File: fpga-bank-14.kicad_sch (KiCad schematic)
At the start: 1 part, among them U1 XC7K410T-2FFG900I

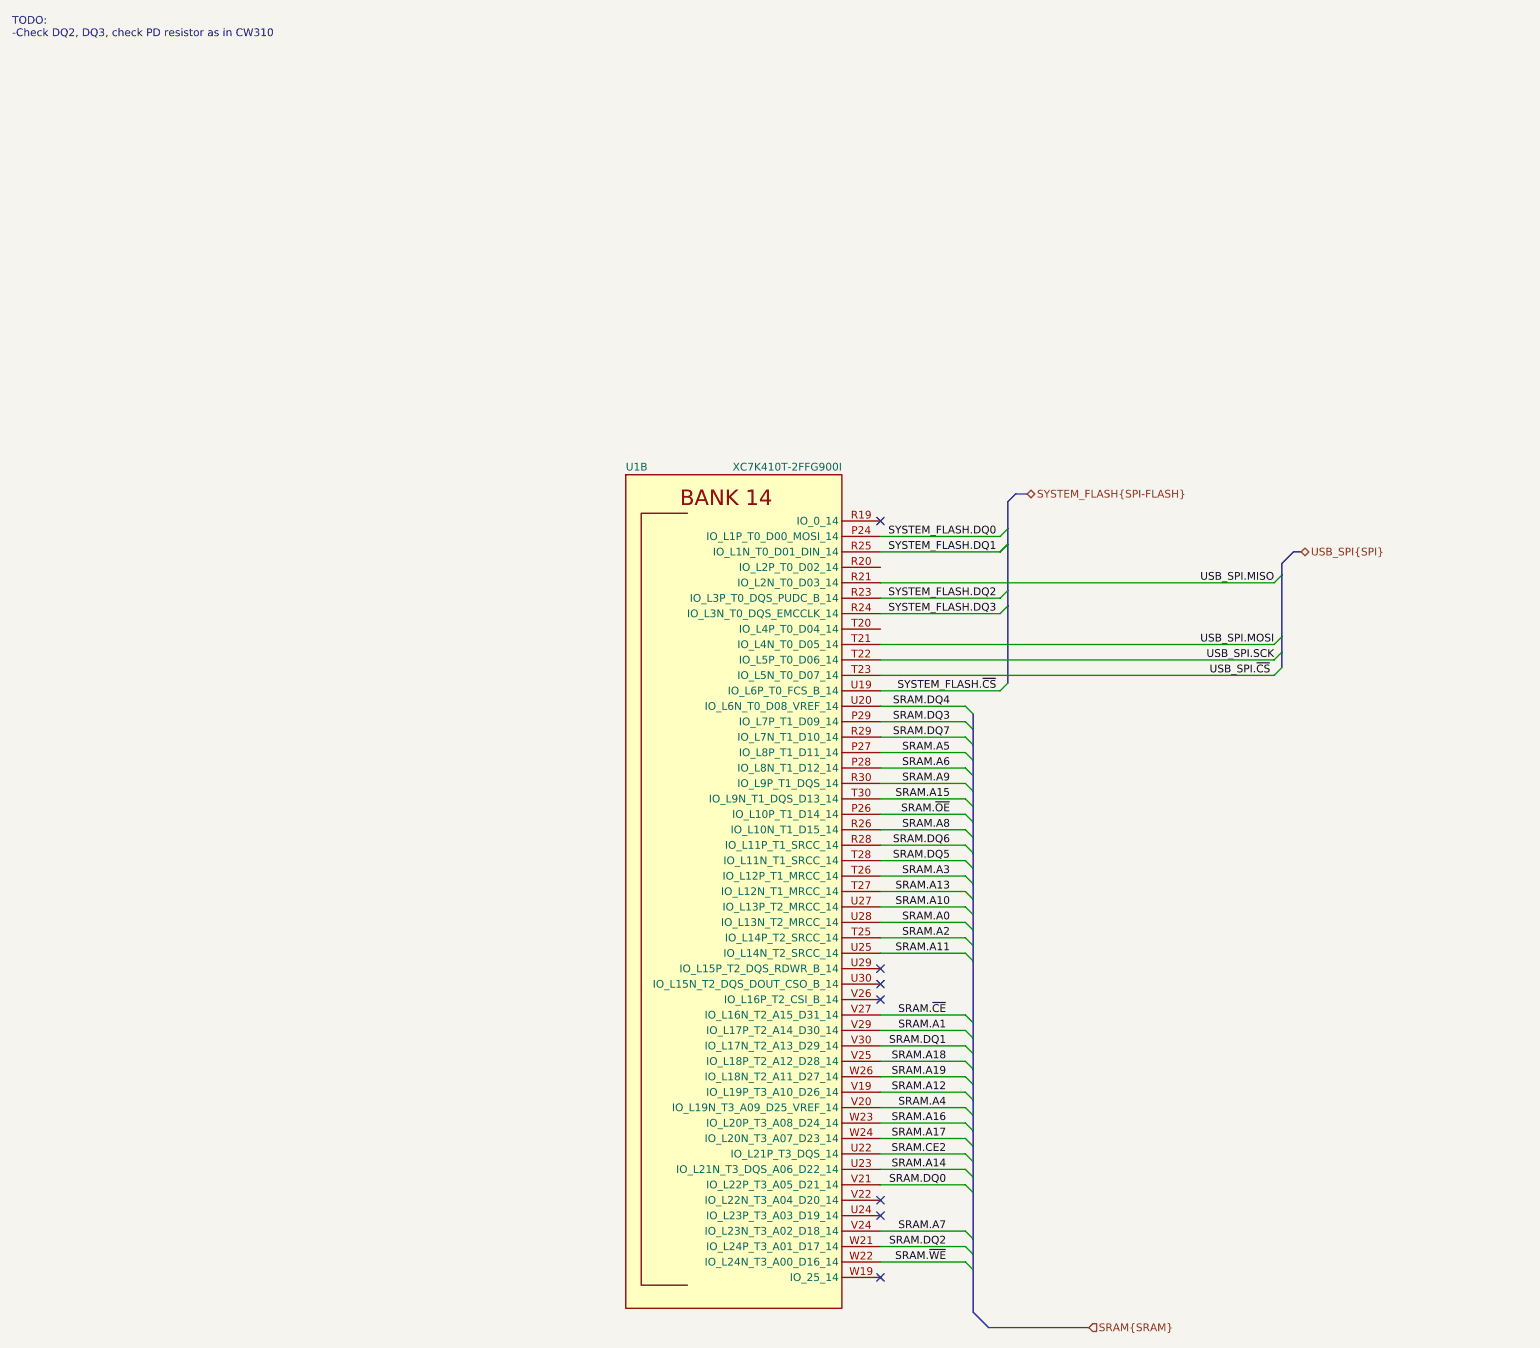
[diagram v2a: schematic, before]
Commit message: Fix system-flash connection to FPGA
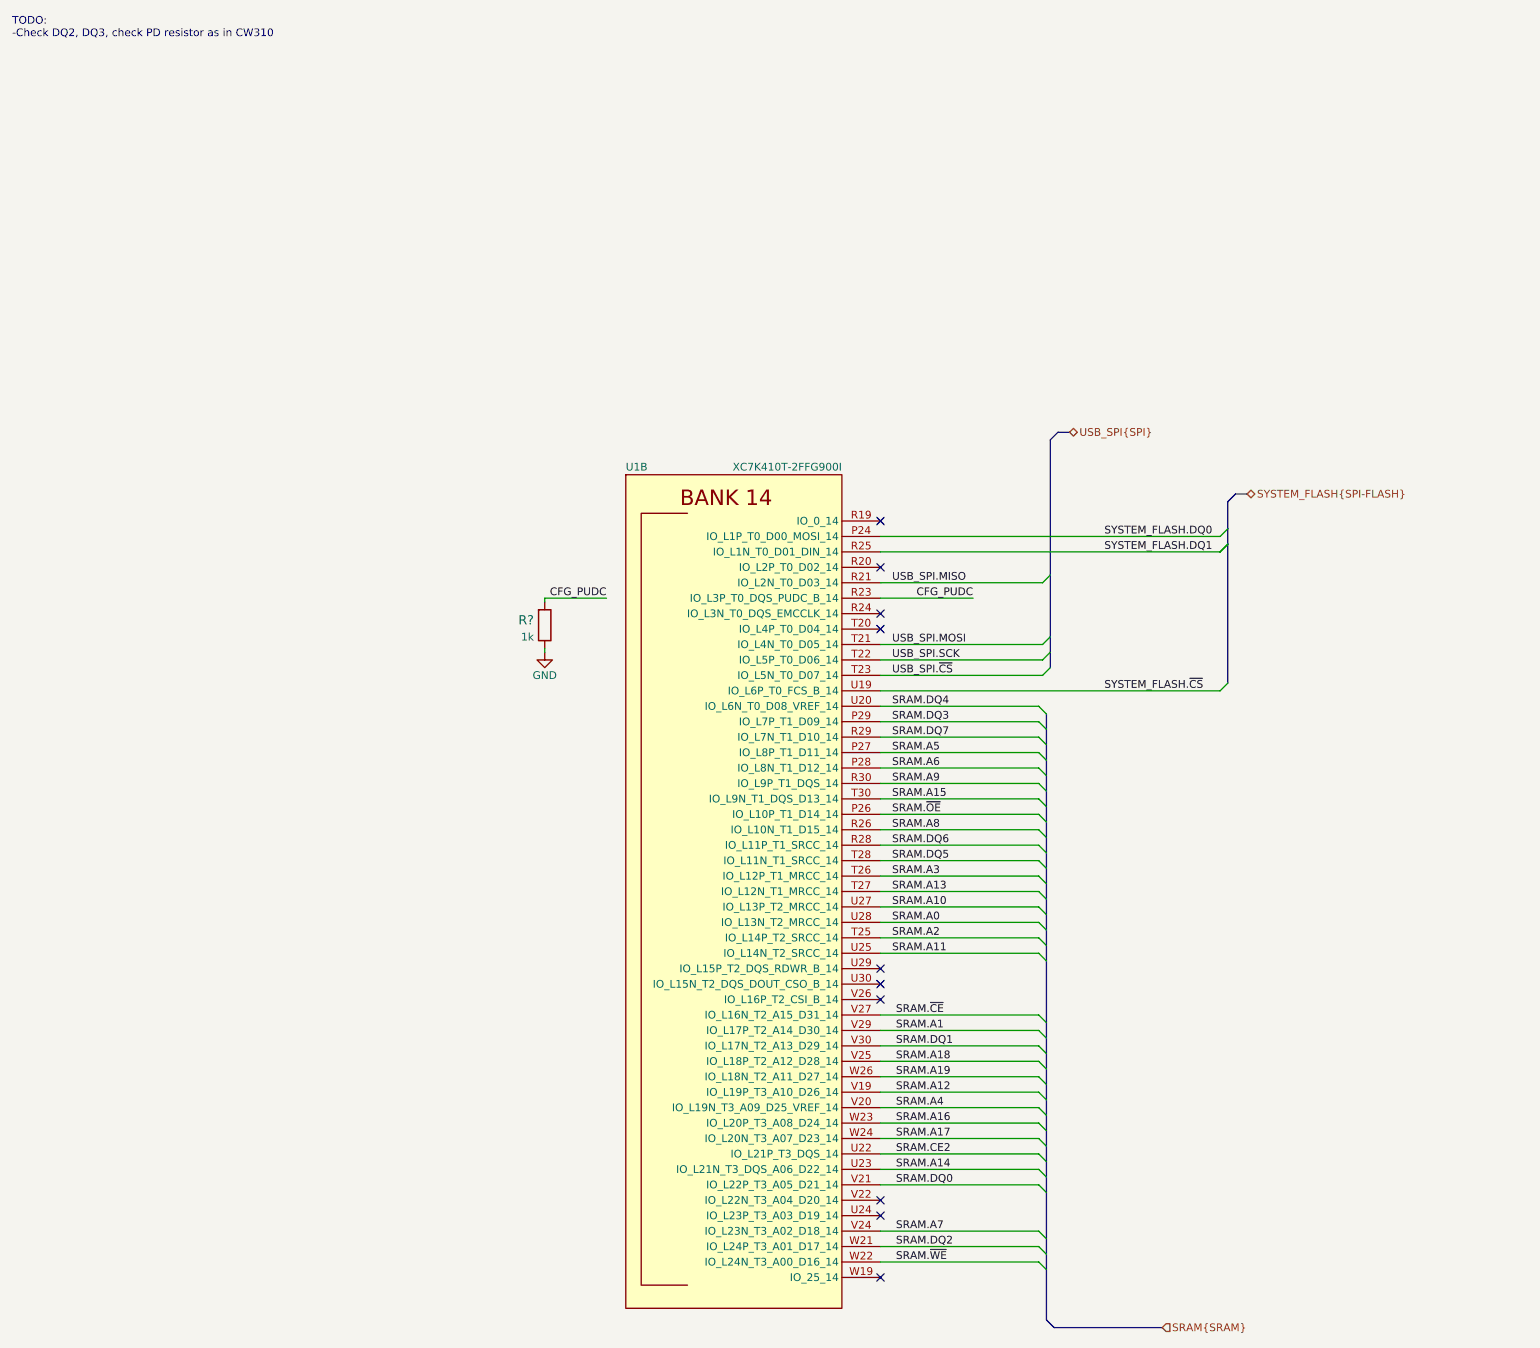
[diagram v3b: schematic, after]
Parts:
- added R?: R_1k_0402, antmicro-footprints:0402-res, symbol antmicroResistors0402:R_1k_0402
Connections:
- net SYSTEM_FLASH.DQ2 renamed CFG_PUDC
- net CFG_PUDC: now also R?.2
- net SYSTEM_FLASH.DQ3: no longer names the net of U1.R24 (IO_L3N_T0_DQS_EMCCLK_14)
- new net GND: R?.1
- no-connect marks 7 -> 10

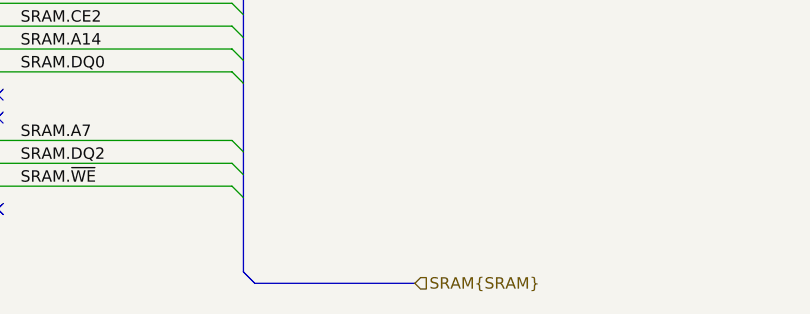
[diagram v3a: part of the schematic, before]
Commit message: Connect USB_HOST on root schematic
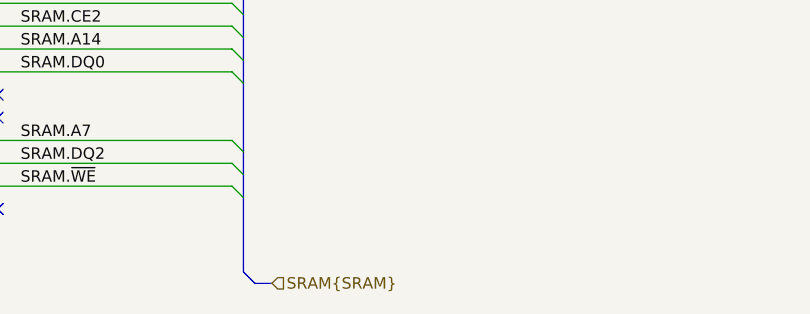
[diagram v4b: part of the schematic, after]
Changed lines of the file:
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@@
     (stroke (width 0) (type default) (color 0 0 0 0))
   )
-  (bus (pts (xy 172.085 216.535) (xy 189.865 216.535))
+  (bus (pts (xy 172.085 216.535) (xy 173.99 216.535))
     (stroke (width 0) (type default) (color 0 0 0 0))
   )
@@
     (stroke (width 0) (type default) (color 0 0 0 0))
   )
+  (bus (pts (xy 170.815 156.21) (xy 170.815 166.37))
+    (stroke (width 0) (type default) (color 0 0 0 0))
+  )
+  (bus (pts (xy 172.72 69.215) (xy 174.625 69.215))
+    (stroke (width 0) (type default) (color 0 0 0 0))
+  )
+  (bus (pts (xy 170.815 179.07) (xy 170.815 181.61))
+    (stroke (width 0) (type default) (color 0 0 0 0))
+  )
+  (wire (pts (xy 143.51 170.18) (xy 169.545 170.18))
+    (stroke (width 0) (type default) (color 0 0 0 0))
+  )
+  (bus (pts (xy 170.815 184.15) (xy 170.815 186.69))
+    (stroke (width 0) (type default) (color 0 0 0 0))
+  )
+  (bus (pts (xy 171.45 70.485) (xy 172.72 69.215))
+    (stroke (width 0) (type default) (color 0 0 0 0))
+  )
+  (wire (pts (xy 143.51 205.74) (xy 169.545 205.74))
+    (stroke (width 0) (type default) (color 0 0 0 0))
+  )
+  (bus (pts (xy 170.815 125.73) (xy 170.815 128.27))
+    (stroke (width 0) (type default) (color 0 0 0 0))
+  )
+  (wire (pts (xy 88.265 96.52) (xy 88.265 97.155))
+    (stroke (width 0) (type default) (color 0 0 0 0))
+  )
+  (bus (pts (xy 170.815 173.99) (xy 170.815 176.53))
+    (stroke (width 0) (type default) (color 0 0 0 0))
+  )
+  (wire (pts (xy 143.51 132.08) (xy 169.545 132.08))
+    (stroke (width 0) (type default) (color 0 0 0 0))
+  )
+  (bus (pts (xy 170.815 148.59) (xy 170.815 151.13))
+    (stroke (width 0) (type default) (color 0 0 0 0))
+  )
+  (wire (pts (xy 88.265 96.52) (xy 98.425 96.52))
+    (stroke (width 0) (type default) (color 0 0 0 0))
+  )
+  (bus (pts (xy 170.815 130.81) (xy 170.815 133.35))
+    (stroke (width 0) (type default) (color 0 0 0 0))
+  )
+  (bus (pts (xy 201.93 79.375) (xy 203.835 79.375))
+    (stroke (width 0) (type default) (color 0 0 0 0))
+  )
+  (bus (pts (xy 171.45 92.71) (xy 171.45 102.87))
+    (stroke (width 0) (type default) (color 0 0 0 0))
+  )
+  (bus (pts (xy 170.815 151.13) (xy 170.815 153.67))
+    (stroke (width 0) (type default) (color 0 0 0 0))
+  )
+  (wire (pts (xy 143.51 134.62) (xy 169.545 134.62))
+    (stroke (width 0) (type default) (color 0 0 0 0))
+  )
+  (bus (pts (xy 200.66 80.645) (xy 200.66 85.09))
+    (stroke (width 0) (type default) (color 0 0 0 0))
+  )
+  (bus (pts (xy 170.815 176.53) (xy 170.815 179.07))
+    (stroke (width 0) (type default) (color 0 0 0 0))
+  )
+  (bus (pts (xy 170.815 120.65) (xy 170.815 123.19))
+    (stroke (width 0) (type default) (color 0 0 0 0))
+  )
+  (bus (pts (xy 170.815 146.05) (xy 170.815 148.59))
+    (stroke (width 0) (type default) (color 0 0 0 0))
+  )
+  (bus (pts (xy 170.815 153.67) (xy 170.815 156.21))
+    (stroke (width 0) (type default) (color 0 0 0 0))
+  )
+  (wire (pts (xy 143.51 124.46) (xy 169.545 124.46))
+    (stroke (width 0) (type default) (color 0 0 0 0))
+  )
+  (bus (pts (xy 170.815 128.27) (xy 170.815 130.81))
+    (stroke (width 0) (type default) (color 0 0 0 0))
+  )
+  (wire (pts (xy 143.51 172.72) (xy 169.545 172.72))
+    (stroke (width 0) (type default) (color 0 0 0 0))
+  )
+  (wire (pts (xy 143.51 165.1) (xy 169.545 165.1))
+    (stroke (width 0) (type default) (color 0 0 0 0))
+  )
+  (bus (pts (xy 200.66 87.63) (xy 200.66 110.49))
+    (stroke (width 0) (type default) (color 0 0 0 0))
+  )
+  (bus (pts (xy 170.815 194.31) (xy 170.815 201.93))
+    (stroke (width 0) (type default) (color 0 0 0 0))
+  )
+  (wire (pts (xy 143.51 104.14) (xy 170.18 104.14))
+    (stroke (width 0) (type default) (color 0 0 0 0))
+  )
   (bus (pts (xy 170.815 207.01) (xy 170.815 215.265))
-    (stroke (width 0) (type default) (color 0 0 0 0))
-  )
-  (bus (pts (xy 170.815 156.21) (xy 170.815 166.37))
-    (stroke (width 0) (type default) (color 0 0 0 0))
-  )
-  (bus (pts (xy 172.72 69.215) (xy 174.625 69.215))
-    (stroke (width 0) (type default) (color 0 0 0 0))
-  )
-  (bus (pts (xy 170.815 179.07) (xy 170.815 181.61))
-    (stroke (width 0) (type default) (color 0 0 0 0))
-  )
-  (wire (pts (xy 143.51 170.18) (xy 169.545 170.18))
-    (stroke (width 0) (type default) (color 0 0 0 0))
-  )
-  (bus (pts (xy 170.815 184.15) (xy 170.815 186.69))
-    (stroke (width 0) (type default) (color 0 0 0 0))
-  )
-  (bus (pts (xy 171.45 70.485) (xy 172.72 69.215))
-    (stroke (width 0) (type default) (color 0 0 0 0))
-  )
-  (wire (pts (xy 143.51 205.74) (xy 169.545 205.74))
-    (stroke (width 0) (type default) (color 0 0 0 0))
-  )
-  (bus (pts (xy 170.815 125.73) (xy 170.815 128.27))
-    (stroke (width 0) (type default) (color 0 0 0 0))
-  )
-  (wire (pts (xy 88.265 96.52) (xy 88.265 97.155))
-    (stroke (width 0) (type default) (color 0 0 0 0))
-  )
-  (bus (pts (xy 170.815 173.99) (xy 170.815 176.53))
-    (stroke (width 0) (type default) (color 0 0 0 0))
-  )
-  (wire (pts (xy 143.51 132.08) (xy 169.545 132.08))
-    (stroke (width 0) (type default) (color 0 0 0 0))
-  )
-  (bus (pts (xy 170.815 148.59) (xy 170.815 151.13))
-    (stroke (width 0) (type default) (color 0 0 0 0))
-  )
-  (wire (pts (xy 88.265 96.52) (xy 98.425 96.52))
-    (stroke (width 0) (type default) (color 0 0 0 0))
-  )
-  (bus (pts (xy 170.815 130.81) (xy 170.815 133.35))
-    (stroke (width 0) (type default) (color 0 0 0 0))
-  )
-  (bus (pts (xy 201.93 79.375) (xy 203.835 79.375))
-    (stroke (width 0) (type default) (color 0 0 0 0))
-  )
-  (bus (pts (xy 171.45 92.71) (xy 171.45 102.87))
-    (stroke (width 0) (type default) (color 0 0 0 0))
-  )
-  (bus (pts (xy 170.815 151.13) (xy 170.815 153.67))
-    (stroke (width 0) (type default) (color 0 0 0 0))
-  )
-  (wire (pts (xy 143.51 134.62) (xy 169.545 134.62))
-    (stroke (width 0) (type default) (color 0 0 0 0))
-  )
-  (bus (pts (xy 200.66 80.645) (xy 200.66 85.09))
-    (stroke (width 0) (type default) (color 0 0 0 0))
-  )
-  (bus (pts (xy 170.815 176.53) (xy 170.815 179.07))
-    (stroke (width 0) (type default) (color 0 0 0 0))
-  )
-  (bus (pts (xy 170.815 120.65) (xy 170.815 123.19))
-    (stroke (width 0) (type default) (color 0 0 0 0))
-  )
-  (bus (pts (xy 170.815 146.05) (xy 170.815 148.59))
-    (stroke (width 0) (type default) (color 0 0 0 0))
-  )
-  (bus (pts (xy 170.815 153.67) (xy 170.815 156.21))
-    (stroke (width 0) (type default) (color 0 0 0 0))
-  )
-  (wire (pts (xy 143.51 124.46) (xy 169.545 124.46))
-    (stroke (width 0) (type default) (color 0 0 0 0))
-  )
-  (bus (pts (xy 170.815 128.27) (xy 170.815 130.81))
-    (stroke (width 0) (type default) (color 0 0 0 0))
-  )
-  (wire (pts (xy 143.51 172.72) (xy 169.545 172.72))
-    (stroke (width 0) (type default) (color 0 0 0 0))
-  )
-  (wire (pts (xy 143.51 165.1) (xy 169.545 165.1))
-    (stroke (width 0) (type default) (color 0 0 0 0))
-  )
-  (bus (pts (xy 200.66 87.63) (xy 200.66 110.49))
-    (stroke (width 0) (type default) (color 0 0 0 0))
-  )
-  (bus (pts (xy 170.815 194.31) (xy 170.815 201.93))
-    (stroke (width 0) (type default) (color 0 0 0 0))
-  )
-  (wire (pts (xy 143.51 104.14) (xy 170.18 104.14))
     (stroke (width 0) (type default) (color 0 0 0 0))
   )
@@
     (effects (font (size 1.27 1.27)) (justify right bottom))
   )
-  (hierarchical_label "SRAM{SRAM}" (shape input) (at 189.865 216.535 0)
+  (hierarchical_label "SRAM{SRAM}" (shape input) (at 173.99 216.535 0)
     (effects (font (size 1.27 1.27)) (justify left))
   )

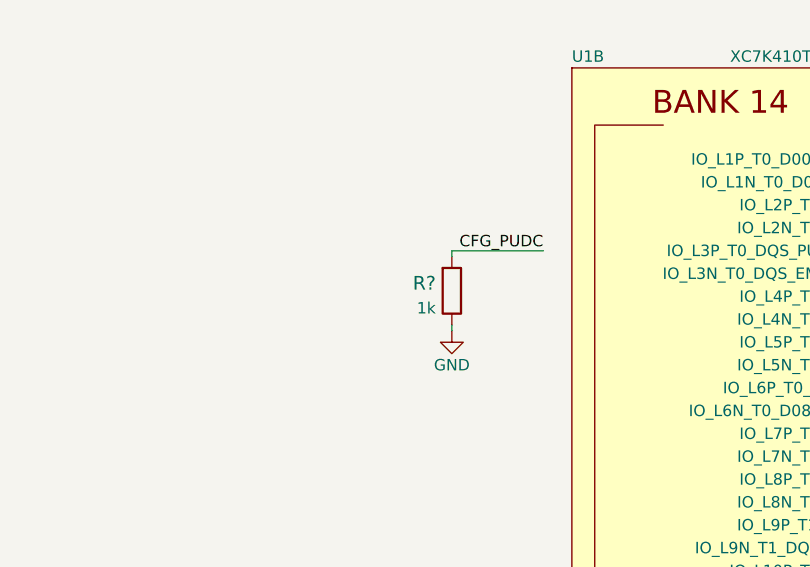
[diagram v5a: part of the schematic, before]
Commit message: Re-annotate the schematic. Export changes to PCB
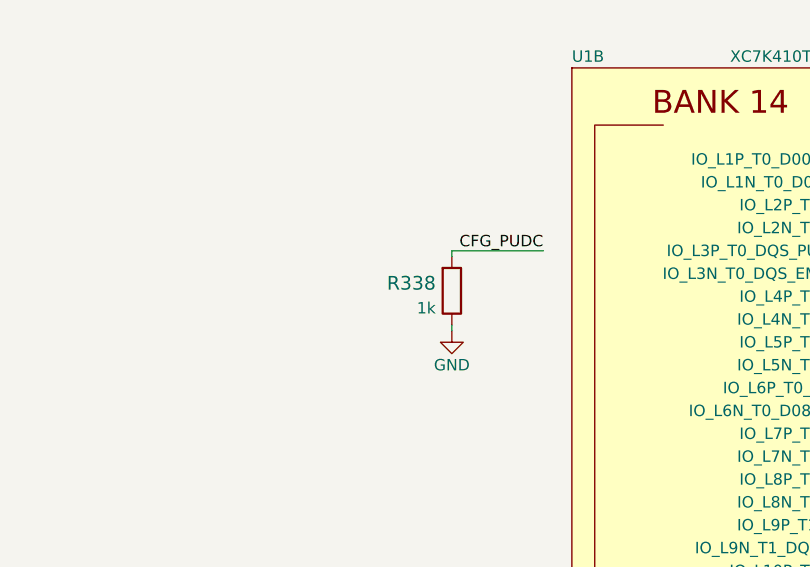
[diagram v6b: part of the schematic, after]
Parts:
- gave numbers to parts that had none: 1
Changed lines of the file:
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@@
   (symbol (lib_id "antmicroResistors0402:R_1k_0402") (at 88.265 100.965 270) (mirror x) (unit 1)
     (in_bom yes) (on_board yes) (fields_autoplaced)
-    (property "Reference" "R?" (id 0) (at 86.487 100.1304 90)
+    (property "Reference" "R338" (id 0) (at 86.487 100.1304 90)
       (effects (font (size 1.524 1.524)) (justify right))
     )
@@
   (symbol (lib_id "power:GND") (at 88.265 105.41 0) (mirror y) (unit 1)
     (in_bom yes) (on_board yes)
-    (property "Reference" "#PWR0526" (id 0) (at 88.265 111.76 0)
+    (property "Reference" "#PWR0420" (id 0) (at 88.265 111.76 0)
       (effects (font (size 1.27 1.27)) hide)
     )
